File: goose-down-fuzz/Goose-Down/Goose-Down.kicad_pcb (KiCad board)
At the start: 2 copper layers, 44.1 x 41.8 mm, 45 parts, among them Q1 BC104, Q2 BC104, Q3 2n5458, Q4 2n5088, U1 LM741, U2 LM741

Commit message: Update tracks
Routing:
- net Net-(C12-Pad1): track 25.0 -> 33.7 mm, vias 0 -> 2
- net Net-(C9-Pad1): track 37.3 -> 39.4 mm
- net Net-(J2-Pad1): track 47.8 -> 49.3 mm
- net Net-(C1-Pad2): track 14.5 -> 15.8 mm
- net Net-(C7-Pad1): track 46.4 -> 47.0 mm

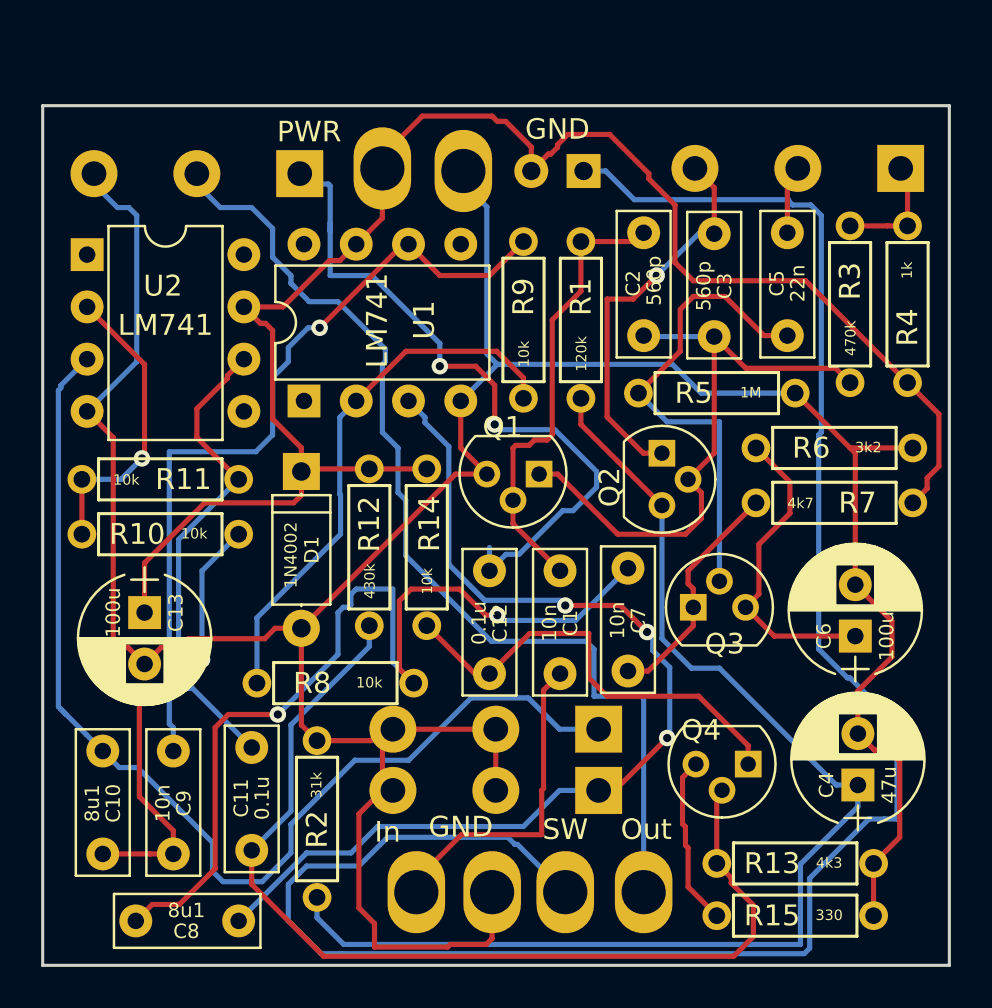
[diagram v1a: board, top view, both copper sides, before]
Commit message: Update GD with Var-resistor Gain wiring, add Tone Stack to LTSpice plot
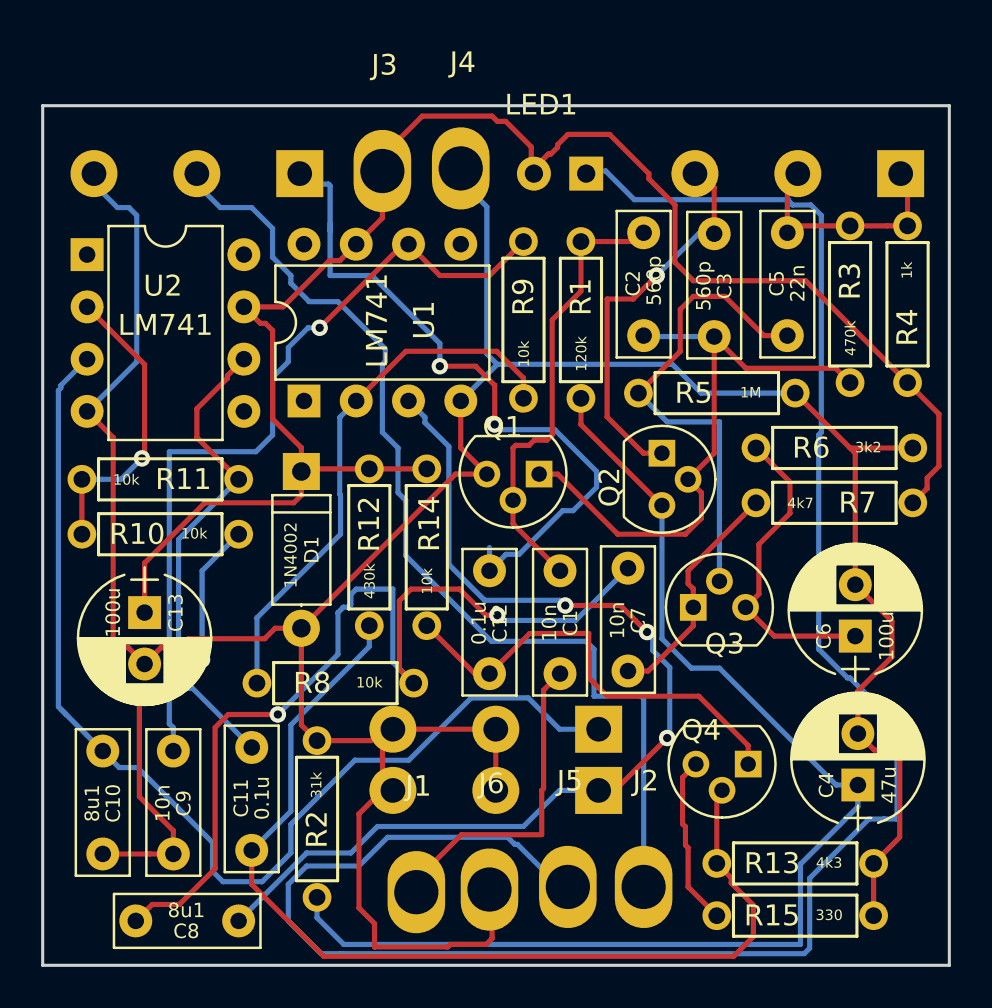
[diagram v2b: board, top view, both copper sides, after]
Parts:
- removed 10kB: Frequency, 4ms_Potentiometer:Pot_Dual_16mm_NoDet_RV16AF-4A
- removed 125kB: Gain, 4ms_Potentiometer:Pot_16mm_NoDet_RV16AF-4A
- removed ?: LED, 4ms-footprints:LED-C1-A2-3MM-VERT
- removed GND (x2): GND, 4ms_Connector:Wire_12AWG
- removed In: In, 4ms_Connector:Wire_12AWG
- removed Out: Out, 4ms_Connector:Wire_12AWG
- removed PWR: PWR, 4ms_Connector:Wire_12AWG
- removed SW: SW, 4ms_Connector:Wire_12AWG
- added J1: In, 4ms_Connector:Wire_12AWG, F.Cu at (166.0, 111.5)
- added J2: Out, 4ms_Connector:Wire_12AWG, F.Cu at (177.0, 111.3)
- added J3: PWR, 4ms_Connector:Wire_12AWG, F.Cu at (164.3, 76.5)
- added J4: GND, 4ms_Connector:Wire_12AWG, F.Cu at (168.1, 76.3)
- added J5: SW, 4ms_Connector:Wire_12AWG, F.Cu at (173.4, 111.3)
- added J6: GND, 4ms_Connector:Wire_12AWG, F.Cu at (169.5, 111.4)
- added LED1: LED, 4ms-footprints:LED-C1-A2-3MM-VERT, B.Cu at (173.0, 76.6)
- added RV1: Gain 125kB, 4ms_Potentiometer:Pot_16mm_NoDet_RV16AF-4A, B.Cu at (184.5, 63.6)
- added RV2: Frequency, 4ms_Potentiometer:Pot_Dual_16mm_NoDet_RV16AF-4A, B.Cu at (169.9, 90.9)
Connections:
- R3 pad 1: Net-(R3-Pad1) -> Net-(C5-Pad2)
- R4 pad 2: Net-(R3-Pad1) -> Net-(C5-Pad2)
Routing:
- net Net-(C5-Pad2): track 3.34 -> 12.3 mm
- net Net-(R3-Pad1): track 5.73 -> 0.00 mm
